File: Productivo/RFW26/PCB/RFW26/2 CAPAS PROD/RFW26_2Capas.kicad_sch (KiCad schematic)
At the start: 40 parts, among them J1 IN 12V, J10 ESP01, J10 OUT, J11 Receptor RF, J4 Conn_02x04_Counter_Clockwise, J5 Receptor RF, J9 jumpers salida, K2 SANYOU_SRD_Form_C, Q2 MMBT5551L, SW1 RESET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

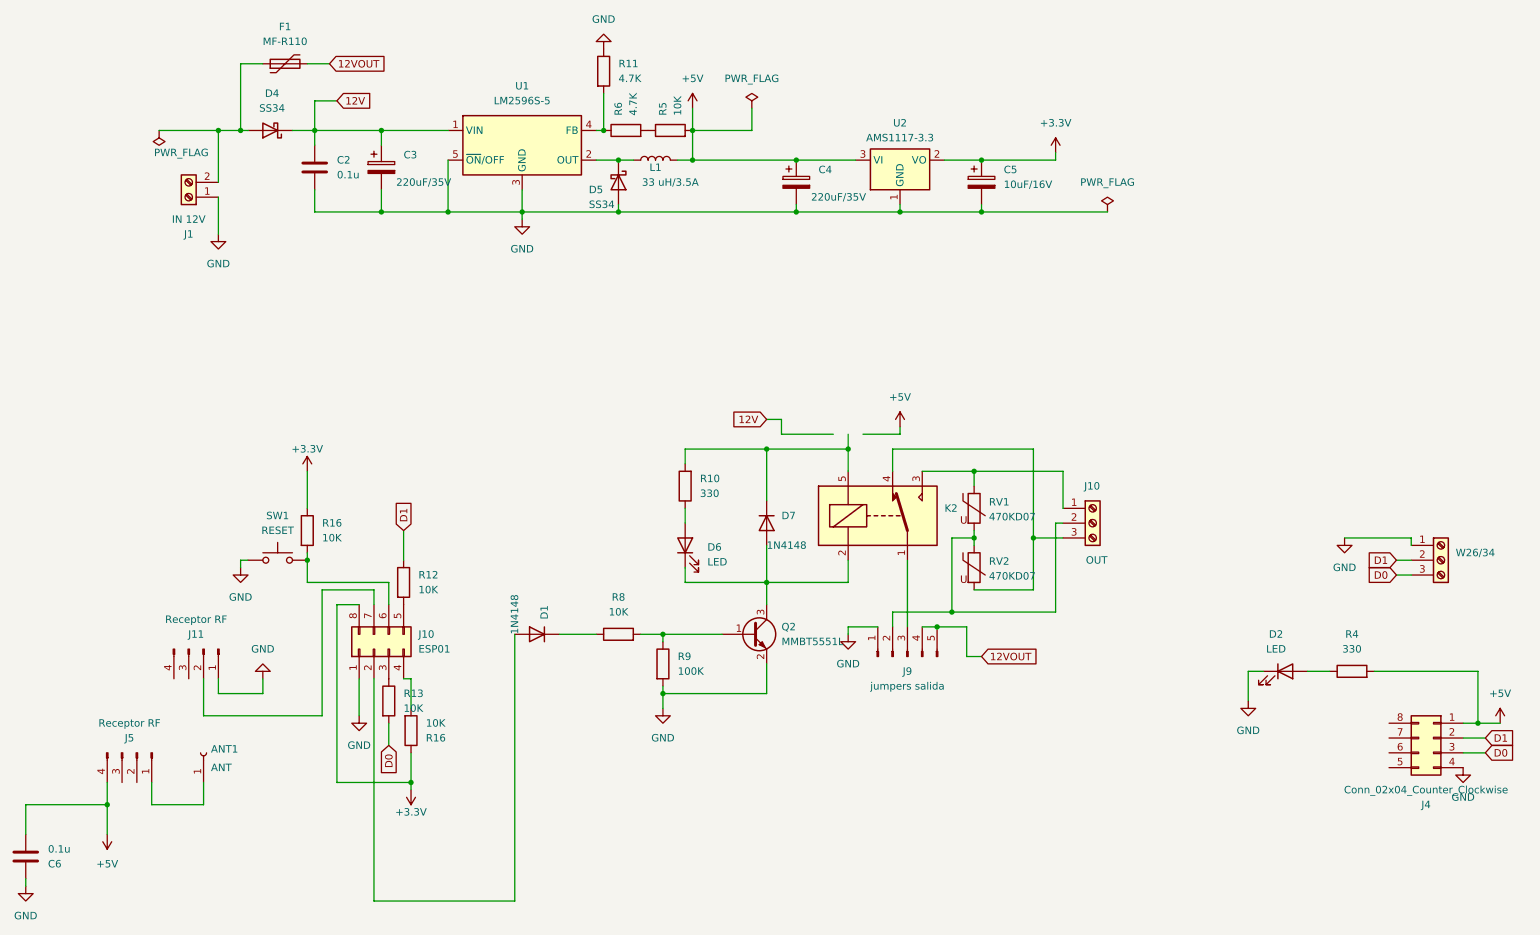
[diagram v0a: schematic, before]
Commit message: Actualizacion de RFW26 a tamaño 80x45
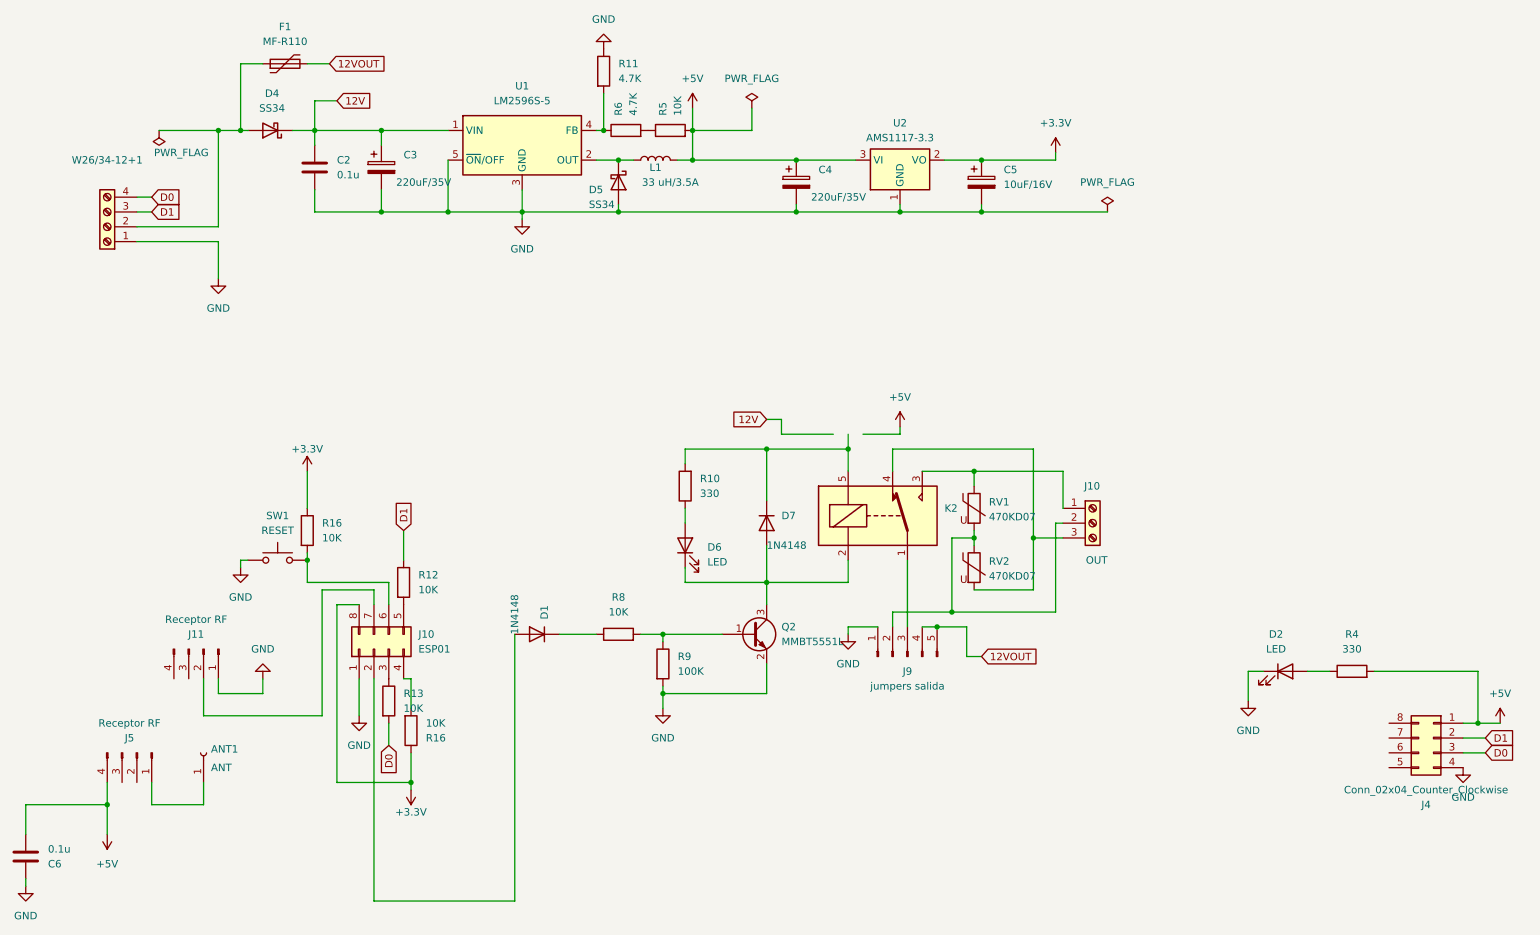
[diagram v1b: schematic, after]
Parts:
- removed J1: IN 12V, TerminalBlock_Phoenix:TerminalBlock_Phoenix_MKDS-1,5-2_1x02_P5.00mm_Horizontal, symbol Connector:Screw_Terminal_01x02
- removed W26/34: Screw_Terminal_01x03, TerminalBlock_Phoenix:TerminalBlock_Phoenix_MKDS-1,5-3_1x03_P5.00mm_Horizontal, symbol Connector:Screw_Terminal_01x03
- added W26/34-12+1: Screw_Terminal_01x04, TerminalBlock_Phoenix:TerminalBlock_Phoenix_MKDS-1,5-4_1x04_P5.00mm_Horizontal, symbol Connector:Screw_Terminal_01x04
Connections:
- net D0: now also W26/34-12+1.4 (Pin_4)
- net D1: now also W26/34-12+1.3 (Pin_3)
- net GND: now also W26/34-12+1.1 (Pin_1)
- net at D4.2 (A), F1.1: now also W26/34-12+1.2 (Pin_2)
